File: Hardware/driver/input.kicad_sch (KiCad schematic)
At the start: 58 parts, among them J302 Würth 74651194R, J303 Würth 74651194R, Q301 IXTH80N075L2, Q302 IXTH80N075L2, U301 MCP3421A2T-ECH, U303 DAC60501Z, U304 LM431SC, U305 MCP3421A3T-ECH, U307 DAC60501Z, U308 LM431SC, U309 DS18B20, U310 DS18B20

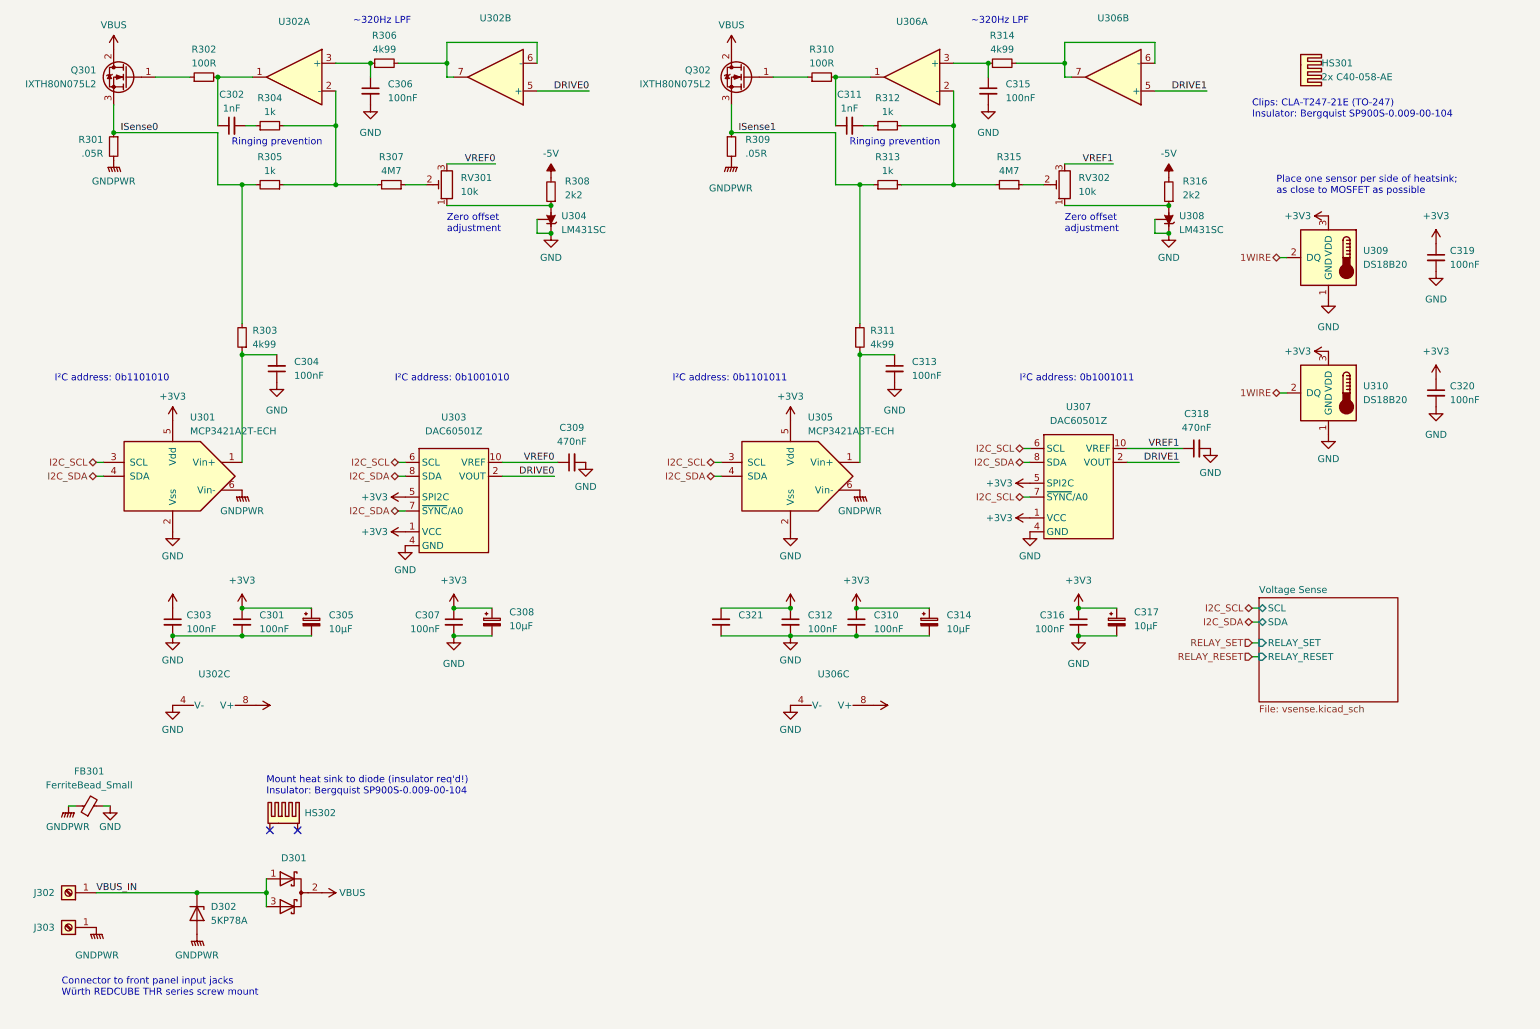
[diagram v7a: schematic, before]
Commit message: More work on rev2 driver board
- Tweaked the board layout for the load driver some more, primarily
  relating to power and friends

- Fixed footprint of fan connector on driver board (to properly have the
  mechanical mounting hole)

- Manufacturability/solderability tweaks for a few other footprints
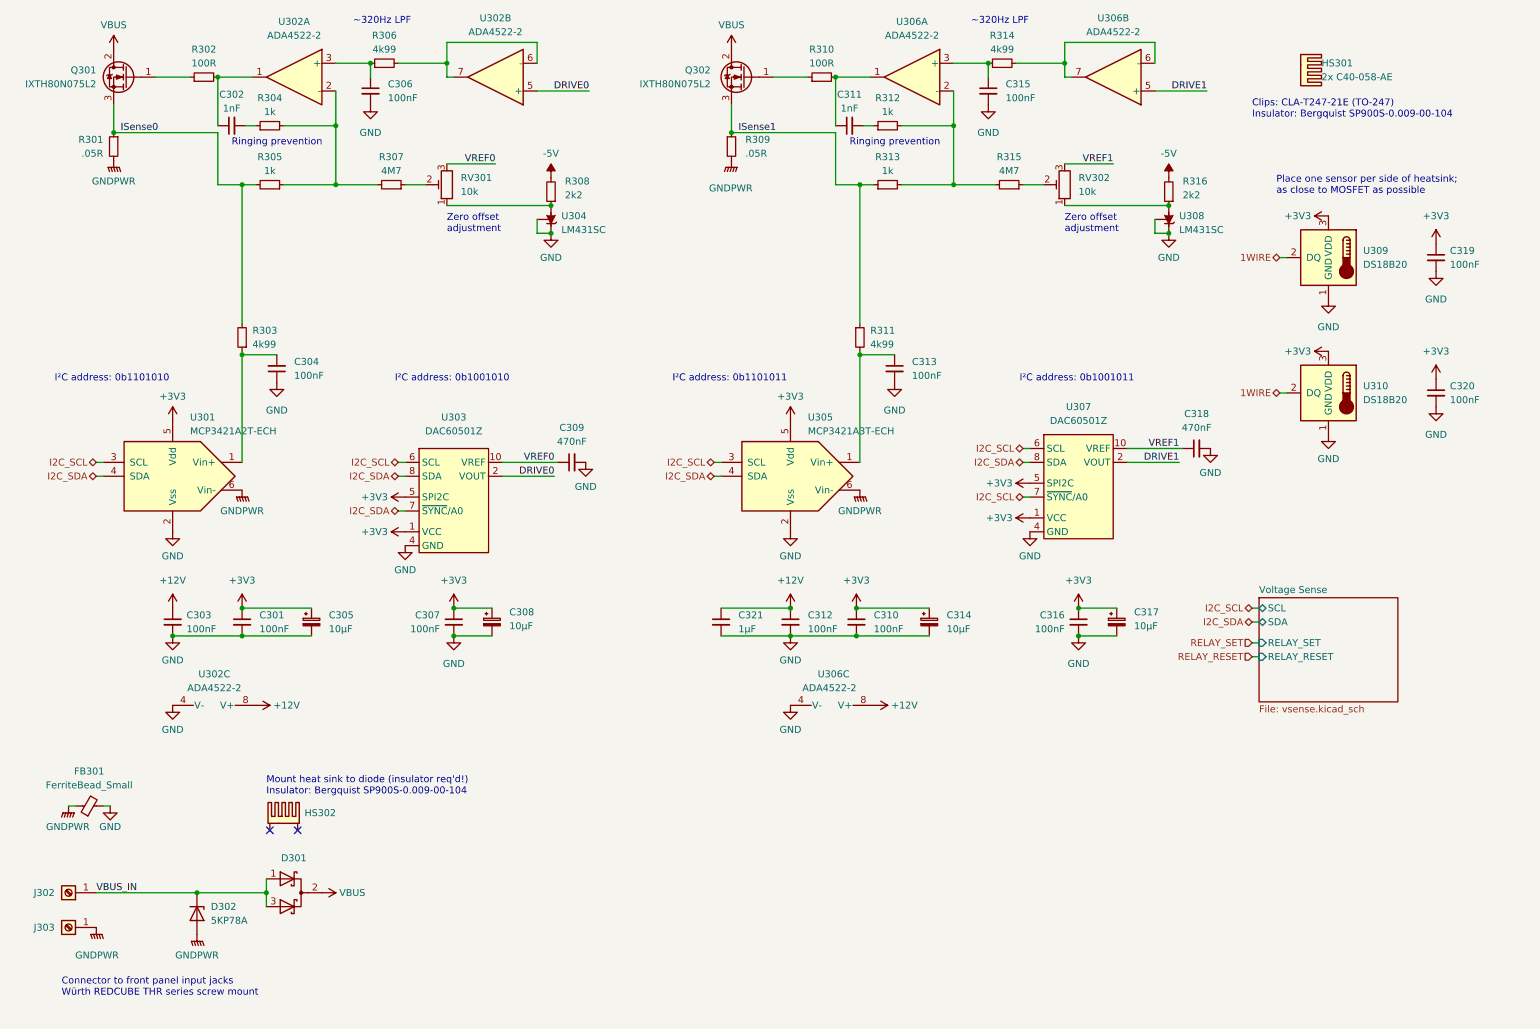
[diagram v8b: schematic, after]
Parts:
- C321: value (none) -> 1µF; footprint (none) -> Capacitor_SMD:C_0805_2012Metric_Pad1.18x1.45mm_HandSolder
- U302, U306: value (none) -> ADA4522-2; footprint (none) -> Package_SO:SOIC-8_3.9x4.9mm_P1.27mm
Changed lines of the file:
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@@
     (in_bom yes) (on_board yes) (fields_autoplaced)
     (property "Reference" "U302" (id 0) (at 64.77 15.24 0))
-    (property "Value" "" (id 1) (at 64.77 17.78 0))
-    (property "Footprint" "" (id 2) (at 64.77 25.4 0)
+    (property "Value" "ADA4522-2" (id 1) (at 64.77 17.78 0))
+    (property "Footprint" "Package_SO:SOIC-8_3.9x4.9mm_P1.27mm" (id 2) (at 64.77 25.4 0)
       (effects (font (size 1.27 1.27)) hide)
     )
@@
     (in_bom yes) (on_board yes) (fields_autoplaced)
     (property "Reference" "U306" (id 0) (at 177.8 15.24 0))
-    (property "Value" "" (id 1) (at 177.8 17.78 0))
-    (property "Footprint" "" (id 2) (at 177.8 25.4 0)
+    (property "Value" "ADA4522-2" (id 1) (at 177.8 17.78 0))
+    (property "Footprint" "Package_SO:SOIC-8_3.9x4.9mm_P1.27mm" (id 2) (at 177.8 25.4 0)
       (effects (font (size 1.27 1.27)) hide)
     )
@@
     (in_bom yes) (on_board yes) (fields_autoplaced)
     (property "Reference" "U302" (id 0) (at 101.6 14.605 0))
-    (property "Value" "" (id 1) (at 101.6 17.145 0))
-    (property "Footprint" "" (id 2) (at 101.6 25.4 0)
+    (property "Value" "ADA4522-2" (id 1) (at 101.6 17.145 0))
+    (property "Footprint" "Package_SO:SOIC-8_3.9x4.9mm_P1.27mm" (id 2) (at 101.6 25.4 0)
       (effects (font (size 1.27 1.27)) hide)
     )
@@
     (in_bom yes) (on_board yes) (fields_autoplaced)
     (property "Reference" "U302" (id 0) (at 50.165 134.62 90))
-    (property "Value" "" (id 1) (at 50.165 137.16 90))
-    (property "Footprint" "" (id 2) (at 50.165 142.875 0)
+    (property "Value" "ADA4522-2" (id 1) (at 50.165 137.16 90))
+    (property "Footprint" "Package_SO:SOIC-8_3.9x4.9mm_P1.27mm" (id 2) (at 50.165 142.875 0)
       (effects (font (size 1.27 1.27)) hide)
     )
@@
     (in_bom yes) (on_board yes) (fields_autoplaced)
     (property "Reference" "U306" (id 0) (at 214.63 14.605 0))
-    (property "Value" "" (id 1) (at 214.63 17.145 0))
-    (property "Footprint" "" (id 2) (at 214.63 25.4 0)
+    (property "Value" "ADA4522-2" (id 1) (at 214.63 17.145 0))
+    (property "Footprint" "Package_SO:SOIC-8_3.9x4.9mm_P1.27mm" (id 2) (at 214.63 25.4 0)
       (effects (font (size 1.27 1.27)) hide)
     )
@@
       (effects (font (size 1.27 1.27)) (justify right))
     )
-    (property "Value" "" (id 1) (at 167.64 137.16 90)
-      (effects (font (size 1.27 1.27)) (justify right))
-    )
-    (property "Footprint" "" (id 2) (at 163.195 142.875 0)
+    (property "Value" "ADA4522-2" (id 1) (at 167.64 137.16 90)
+      (effects (font (size 1.27 1.27)) (justify right))
+    )
+    (property "Footprint" "Package_SO:SOIC-8_3.9x4.9mm_P1.27mm" (id 2) (at 163.195 142.875 0)
       (effects (font (size 1.27 1.27)) hide)
     )
@@
       (effects (font (size 1.27 1.27)) hide)
     )
-    (property "Value" "" (id 1) (at 42.545 117.475 0))
+    (property "Value" "+12V" (id 1) (at 42.545 117.475 0))
     (property "Footprint" "" (id 2) (at 42.545 122.555 0)
       (effects (font (size 1.27 1.27)) hide)
@@
       (effects (font (size 1.27 1.27)) hide)
     )
-    (property "Value" "" (id 1) (at 60.96 140.3349 90)
+    (property "Value" "+12V" (id 1) (at 60.96 140.3349 90)
       (effects (font (size 1.27 1.27)) (justify left))
     )
@@
       (effects (font (size 1.27 1.27)) hide)
     )
-    (property "Value" "" (id 1) (at 155.575 117.475 0))
+    (property "Value" "+12V" (id 1) (at 155.575 117.475 0))
     (property "Footprint" "" (id 2) (at 155.575 122.555 0)
       (effects (font (size 1.27 1.27)) hide)
@@
       (effects (font (size 1.27 1.27)) (justify right))
     )
-    (property "Value" "" (id 1) (at 146.05 126.3712 0)
-      (effects (font (size 1.27 1.27)) (justify right))
-    )
-    (property "Footprint" "" (id 2) (at 142.875 125.095 0)
+    (property "Value" "1µF" (id 1) (at 146.05 126.3712 0)
+      (effects (font (size 1.27 1.27)) (justify right))
+    )
+    (property "Footprint" "Capacitor_SMD:C_0805_2012Metric_Pad1.18x1.45mm_HandSolder" (id 2) (at 142.875 125.095 0)
       (effects (font (size 1.27 1.27)) hide)
     )
@@
       (effects (font (size 1.27 1.27)) hide)
     )
-    (property "Value" "" (id 1) (at 173.99 140.3349 90)
-      (effects (font (size 1.27 1.27)) (justify left))
-    )
+    (property "Value" "+12V" (id 1) (at 173.99 140.3349 90)
+      (effects (font (size 1.27 1.27)) (justify left))
+    )
